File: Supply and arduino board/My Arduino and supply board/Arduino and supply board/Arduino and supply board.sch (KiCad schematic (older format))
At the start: 60 parts, among them J1 USB_C_Receptacle_USB2.0, J2 Conn_01x03, J3 Conn_01x03, J4 Conn_01x03, J5 Conn_01x03, J6 Conn_01x03, J7 Conn_01x03, Q2 16MHz, T1 FDN340V, U1 LM358D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

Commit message: work on arduino board
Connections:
- net GND: now also U8.13 (GND), U8.21 (GND)
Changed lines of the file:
@@
 	4650 7250 4650 7400
-Wire Wire Line
-	5550 7850 4850 7850
 Wire Wire Line
 	4650 7850 4650 7700
@@
 	1    0    0    -1
 $EndComp
-Connection ~ 4850 7850
 Wire Wire Line
 	4850 7850 4650 7850
@@
 Wire Wire Line
 	12000 7400 12350 7400
+Wire Wire Line
+	4850 7850 5450 7850
+Connection ~ 4850 7850
+Connection ~ 5450 7850
+Wire Wire Line
+	5450 7850 5550 7850
+Connection ~ 5550 7850
+Wire Wire Line
+	5550 7850 5650 7850
 $EndSCHEMATC

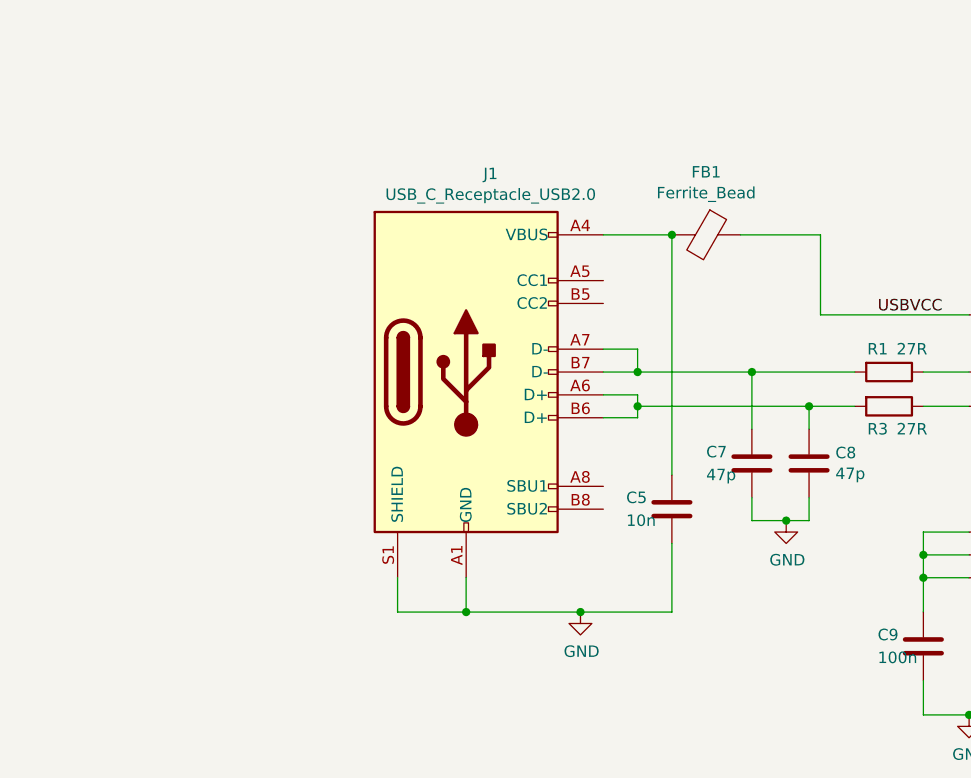
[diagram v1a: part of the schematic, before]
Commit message: add usb protect
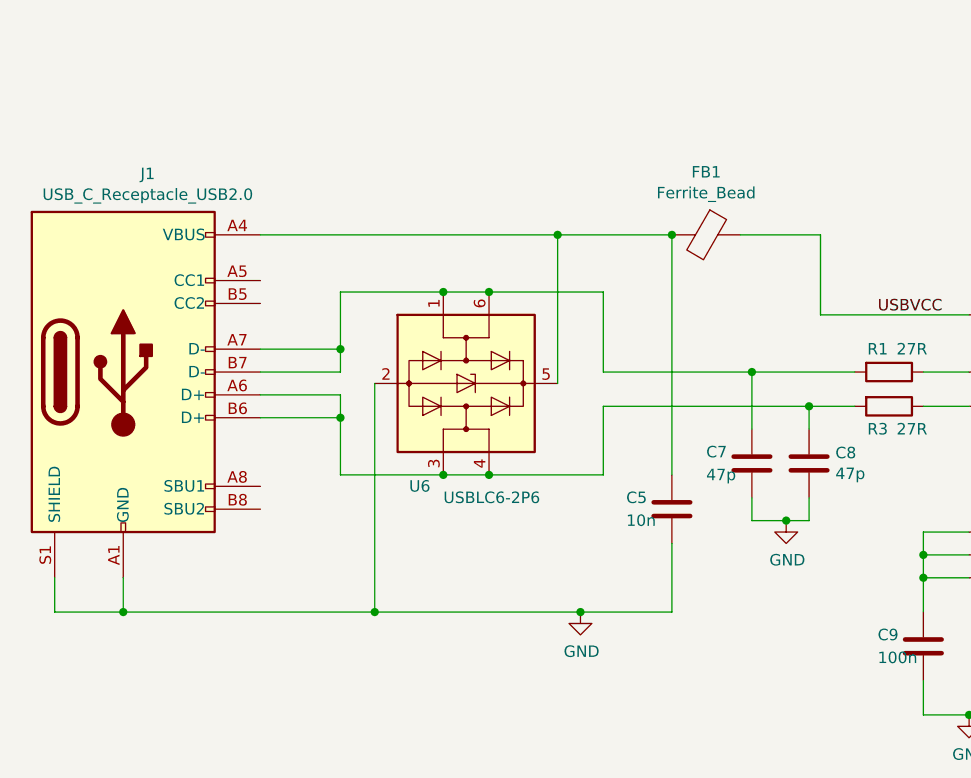
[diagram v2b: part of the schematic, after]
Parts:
- added U6: USBLC6-2P6, Package_TO_SOT_SMD:SOT-666, symbol Power_Protection:USBLC6-2P6
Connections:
- net GND: now also U6.2 (GND)
- net at C5.1, FB1.2, J1.A4 (VBUS)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: now also U6.5 (VBUS)
- net at C8.1, J1.A6 (D+), J1.B6 (D+)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: now also U6.3 (I/O2), U6.4 (I/O2)
- net at C7.1, J1.A7 (D-), J1.B7 (D-)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: now also U6.1 (I/O1), U6.6 (I/O1)
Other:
- moved on the sheet: J1
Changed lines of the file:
@@
 L Connector:USB_C_Receptacle_USB2.0 J1
 U 1 1 657D24C2
-P 2650 6350
-F 0 "J1" H 2757 7217 50  0000 C CNN
-F 1 "USB_C_Receptacle_USB2.0" H 2757 7126 50  0000 C CNN
-F 2 "Connector_USB:USB_C_Receptacle_HRO_TYPE-C-31-M-12" H 2800 6350 50  0001 C CNN
-F 3 "https://www.usb.org/sites/default/files/documents/usb_type-c.zip" H 2800 6350 50  0001 C CNN
-	1    2650 6350
+P 1150 6350
+F 0 "J1" H 1257 7217 50  0000 C CNN
+F 1 "USB_C_Receptacle_USB2.0" H 1257 7126 50  0000 C CNN
+F 2 "Connector_USB:USB_C_Receptacle_HRO_TYPE-C-31-M-12" H 1300 6350 50  0001 C CNN
+F 3 "https://www.usb.org/sites/default/files/documents/usb_type-c.zip" H 1300 6350 50  0001 C CNN
+	1    1150 6350
 	1    0    0    -1
 $EndComp
@@
 $EndComp
 Wire Wire Line
-	3250 5750 3550 5750
-Wire Wire Line
 	4850 6100 4200 6100
 Wire Wire Line
@@
 	4850 6500 4650 6500
 Wire Wire Line
-	3250 6350 3400 6350
-Wire Wire Line
 	4350 6500 4150 6500
-Wire Wire Line
-	3400 6500 3400 6450
-Wire Wire Line
-	3400 6450 3250 6450
-Wire Wire Line
-	3250 6550 3400 6550
-Wire Wire Line
-	3400 6550 3400 6500
-Connection ~ 3400 6500
-Wire Wire Line
-	3250 6250 3400 6250
-Wire Wire Line
-	3400 6250 3400 6350
-Connection ~ 3400 6350
-Wire Wire Line
-	3400 6350 3900 6350
 $Comp
 L power:GND #PWR0107
@@
 USBVCC
 Wire Wire Line
-	2650 7250 2650 7400
-Wire Wire Line
-	2650 7400 3150 7400
-Wire Wire Line
 	3550 7400 3550 7100
 Wire Wire Line
@@
 	3150 7400 3550 7400
 Wire Wire Line
-	2350 7250 2350 7400
-Wire Wire Line
-	2350 7400 2650 7400
-Connection ~ 2650 7400
-Wire Wire Line
 	3900 6600 3900 6350
 Connection ~ 3900 6350
@@
 	4150 6600 4150 6500
 Connection ~ 4150 6500
-Wire Wire Line
-	4150 6500 3400 6500
 Wire Wire Line
 	3900 6900 3900 7000
@@
 Wire Wire Line
 	5550 7850 5650 7850
+$Comp
+L Power_Protection:USBLC6-2P6 U6
+U 1 1 6579E1C3
+P 2650 6400
+F 0 "U6" V 3100 6150 50  0000 L CNN
+F 1 "USBLC6-2P6" V 3150 6300 50  0000 L CNN
+F 2 "Package_TO_SOT_SMD:SOT-666" H 2650 5900 50  0001 C CNN
+F 3 "https://www.st.com/resource/en/datasheet/usblc6-2.pdf" H 2850 6750 50  0001 C CNN
+	1    2650 6400
+	0    1    1    0
+$EndComp
+Wire Wire Line
+	1750 6250 2100 6250
+Wire Wire Line
+	2100 6250 2100 6000
+Wire Wire Line
+	2100 6000 2550 6000
+Connection ~ 2550 6000
+Wire Wire Line
+	2550 6000 2750 6000
+Connection ~ 2750 6000
+Wire Wire Line
+	2750 6000 3250 6000
+Wire Wire Line
+	3250 6000 3250 6350
+Wire Wire Line
+	3250 6350 3900 6350
+Wire Wire Line
+	1750 6350 2100 6350
+Wire Wire Line
+	2100 6350 2100 6250
+Connection ~ 2100 6250
+Wire Wire Line
+	1750 6550 2100 6550
+Wire Wire Line
+	2100 6550 2100 6800
+Wire Wire Line
+	2100 6800 2550 6800
+Connection ~ 2550 6800
+Wire Wire Line
+	2550 6800 2750 6800
+Connection ~ 2750 6800
+Wire Wire Line
+	2750 6800 3250 6800
+Wire Wire Line
+	3250 6500 3250 6800
+Wire Wire Line
+	3250 6500 4150 6500
+Wire Wire Line
+	1750 6450 2100 6450
+Wire Wire Line
+	2100 6450 2100 6550
+Connection ~ 2100 6550
+Wire Wire Line
+	850  7250 850  7400
+Wire Wire Line
+	850  7400 1150 7400
+Wire Wire Line
+	1150 7250 1150 7400
+Connection ~ 1150 7400
+Wire Wire Line
+	1150 7400 2250 7400
+Wire Wire Line
+	1750 5750 3050 5750
+Wire Wire Line
+	2250 6400 2250 7400
+Connection ~ 2250 7400
+Wire Wire Line
+	2250 7400 3150 7400
+Wire Wire Line
+	3050 6400 3050 5750
+Connection ~ 3050 5750
+Wire Wire Line
+	3050 5750 3550 5750
 $EndSCHEMATC

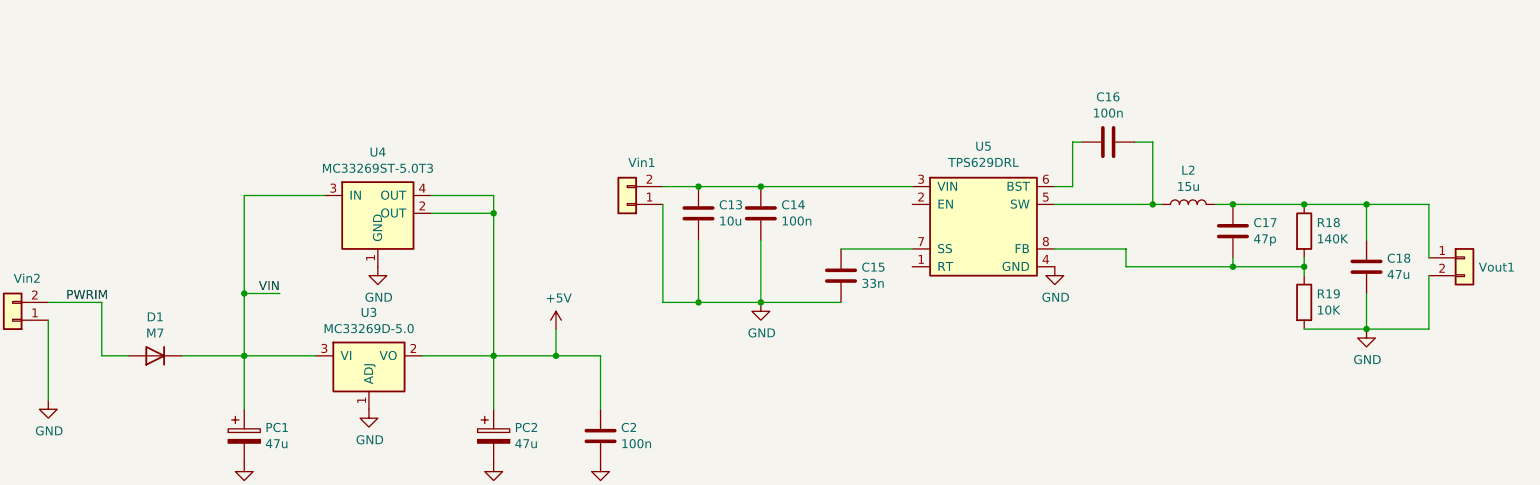
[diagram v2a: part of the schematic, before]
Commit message: add text on PCB
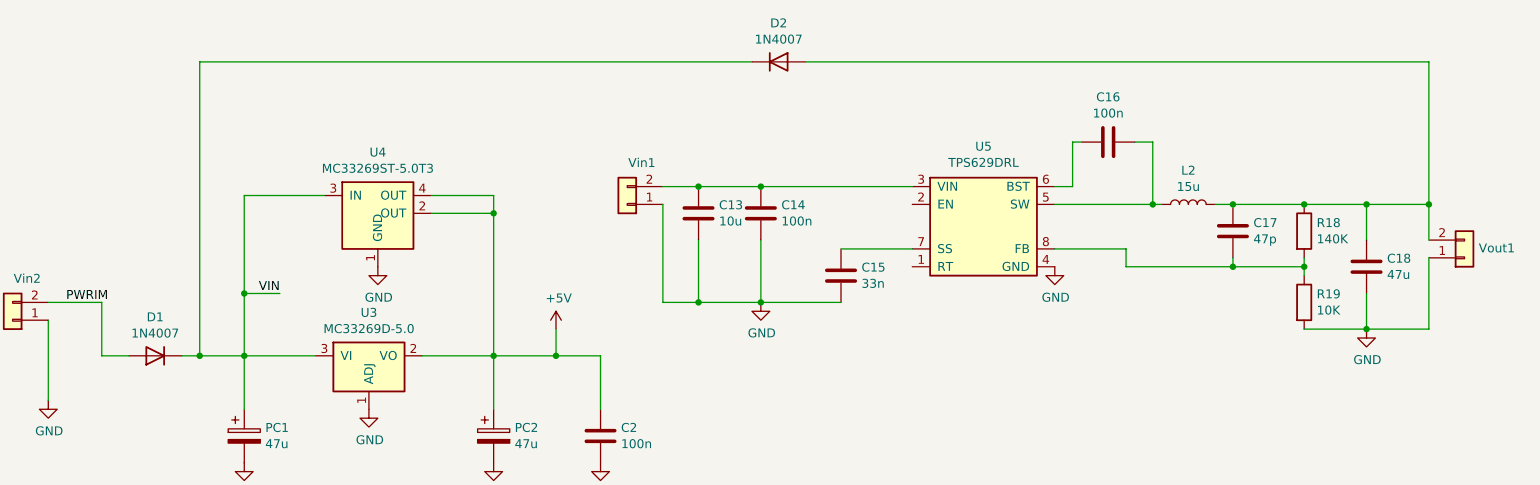
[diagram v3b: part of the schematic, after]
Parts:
- added D2: 1N4007, Diode_SMD:D_SMA, symbol Device:D
- D1: value M7 -> 1N4007; footprint Diode_SMD:D_SMB -> Diode_SMD:D_SMA
- Vin1, Vin2, Vout1: footprint Connector_PinSocket_2.54mm:PinSocket_1x02_P2.54mm_Vertical -> Connector_PinSocket_2.54mm:PinSocket_1x02_P2.54mm_Horizontal
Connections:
- net GND: now also Vout1.1 (Pin_1); no longer Vout1.2 (Pin_2)
- net VIN: now also D2.1 (K)
- net at C17.2, C18.2, L2.2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: now also Vout1.2 (Pin_2), D2.2 (A); no longer Vout1.1 (Pin_1)
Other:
- moved on the sheet: Vout1
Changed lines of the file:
@@
 P 8350 2300
 F 0 "D1" H 8350 2083 50  0000 C CNN
-F 1 "M7" H 8350 2174 50  0000 C CNN
-F 2 "Diode_SMD:D_SMB" H 8350 2300 50  0001 C CNN
+F 1 "1N4007" H 8350 2174 50  0000 C CNN
+F 2 "Diode_SMD:D_SMA" H 8350 2300 50  0001 C CNN
 F 3 "~" H 8350 2300 50  0001 C CNN
 	1    8350 2300
@@
 	8850 2300 9250 2300
 Wire Wire Line
-	8500 2300 8850 2300
+	8500 2300 8600 2300
 Connection ~ 8850 2300
 Wire Wire Line
@@
 F 0 "Vin1" H 10918 1217 50  0000 C CNN
 F 1 "Conn_01x02" H 10918 1216 50  0001 C CNN
-F 2 "Connector_PinSocket_2.54mm:PinSocket_1x02_P2.54mm_Vertical" H 11000 1450 50  0001 C CNN
+F 2 "Connector_PinSocket_2.54mm:PinSocket_1x02_P2.54mm_Horizontal" H 11000 1450 50  0001 C CNN
 F 3 "~" H 11000 1450 50  0001 C CNN
 	1    11000 1450
@@
 F 0 "Vout1" H 15780 1696 50  0000 L CNN
 F 1 "Conn_01x02" H 15780 1651 50  0001 L CNN
-F 2 "Connector_PinSocket_2.54mm:PinSocket_1x02_P2.54mm_Vertical" H 15700 1750 50  0001 C CNN
+F 2 "Connector_PinSocket_2.54mm:PinSocket_1x02_P2.54mm_Horizontal" H 15700 1750 50  0001 C CNN
 F 3 "~" H 15700 1750 50  0001 C CNN
 	1    15700 1750
-	1    0    0    -1
+	1    0    0    1
 $EndComp
 Wire Wire Line
@@
 	14800 1450 15150 1450
 Wire Wire Line
-	15500 1450 15500 1750
+	15500 1450 15500 1650
 Connection ~ 14800 1450
 Wire Wire Line
@@
 Wire Wire Line
 	15150 1450 15500 1450
-Wire Wire Line
-	15500 1850 15500 2150
 Wire Wire Line
 	15500 2150 15150 2150
@@
 F 0 "Vin2" H 7468 1867 50  0000 C CNN
 F 1 "Conn_01x02" H 7468 1866 50  0001 C CNN
-F 2 "Connector_PinSocket_2.54mm:PinSocket_1x02_P2.54mm_Vertical" H 7550 2100 50  0001 C CNN
+F 2 "Connector_PinSocket_2.54mm:PinSocket_1x02_P2.54mm_Horizontal" H 7550 2100 50  0001 C CNN
 F 3 "~" H 7550 2100 50  0001 C CNN
 	1    7550 2100
@@
 Wire Wire Line
 	3050 5750 3550 5750
+$Comp
+L Device:D D2
+U 1 1 657C3DFA
+P 11850 650
+F 0 "D2" H 11850 867 50  0000 C CNN
+F 1 "1N4007" H 11850 776 50  0000 C CNN
+F 2 "Diode_SMD:D_SMA" H 11850 650 50  0001 C CNN
+F 3 "~" H 11850 650 50  0001 C CNN
+	1    11850 650
+	1    0    0    -1
+$EndComp
+Wire Wire Line
+	15500 1450 15500 650
+Wire Wire Line
+	15500 650  12000 650
+Connection ~ 15500 1450
+Wire Wire Line
+	11700 650  8600 650
+Wire Wire Line
+	8600 650  8600 2300
+Connection ~ 8600 2300
+Wire Wire Line
+	8600 2300 8850 2300
+Wire Wire Line
+	15500 1750 15500 2150
 $EndSCHEMATC
